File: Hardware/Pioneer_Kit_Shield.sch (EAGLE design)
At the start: 23 parts, among them J1 AVR_SPI_PRG_6NS, U1 USD-SOCKETNEW, U2 ARDUINO_R3_SHIELDNOLABELS, U3 HEX_CONVERTER

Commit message: Initial post-copy commit
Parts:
- removed J1: AVR_SPI_PRG_6NS, SparkFun-Connectors:AVR_SPI_PRG_6NS
- removed LOGO2: SFE_LOGO_FLAME.6_INCH, SparkFun-Aesthetics:SFE_LOGO_FLAME.6_INCH
- removed U$1: REVISION, SparkFun-Aesthetics:REVISION
- added C4: 0.1uF, SparkFun-Capacitors:0.1UF-0603-25V-5%
- added C5, C6: 1.0uF, SparkFun-Capacitors:1.0UF-0603-16V-10%
- added J2: (no value), SparkFun-Connectors:QWIIC_CONNECTORJS-1MM
- added JP10, JP11: FIDUCIAL1X2, SparkFun-Aesthetics:FIDUCIAL1X2
- added JP8: (no value), SparkFun-RF:XBEESMD
- added JP9: JUMPER-SMT_3_1-NC_PASTE_SILK, SparkFun-Jumpers:JUMPER-SMT_3_1-NC_PASTE_SILK
- added LED2: RED, SparkFun-LED:LED-RED0603
- added R2, R3, R4, R5: 10k, SparkFun-Resistors:10KOHM-0603-1/10W-1%
- added R6: 200k, SparkFun-Resistors:200KOHM-0603-1/10W-1%
- added R7: 1k, SparkFun-Resistors:1KOHM-0603-1/10W-1%
- added S2: (no value), SparkFun:TAC_SWITCHSMD
- added U4: PCA9306, SparkFun-IC-Comms:PCA9306PCA9306DC-1:1
- added U5: 3.3V, SparkFun-IC-Power:V_REG_AP2112K-3.3V
- C1, C2: device SparkFun-Capacitors:0.1UF-25V-5%(0603) -> SparkFun-Capacitors:0.1UF-0603-25V-5%
- C3: device SparkFun-Capacitors:10UF-6.3V-20%(0603) -> SparkFun-Capacitors:10UF-0603-6.3V-20%
- LED1: value Red -> RED; device SparkFun:LED0603 -> SparkFun-LED:LED-RED0603
- R1: device SparkFun:RESISTOR0603-RES -> SparkFun-Resistors:1KOHM-0603-1/10W-1%
- SJ1, SJ2: value SOLDERJUMPERNC -> JUMPER-SMT_2_NC_PASTE_SILK; device SparkFun-Passives:SOLDERJUMPERNC -> SparkFun-Jumpers:JUMPER-SMT_2_NC_PASTE_SILK
- U2: value ARDUINO_R3_SHIELDNOLABELS -> ARDUINO_UNO_R3_SHIELDNOLABELS; device SparkFun-Boards:ARDUINO_R3_SHIELDNOLABELS -> SparkFun-Boards:ARDUINO_UNO_R3_SHIELDNOLABELS
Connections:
- removed net CS: JP5.1, U2.D8, U3.1A
- removed net D10: JP5.3, U2.*D10
- new net !CS: JP5.3, U2.*D10, U3.1A
- new net D8: JP5.1, U2.D8
- new net N$1: LED2.C, R7.2
- new net N$19: R6.1, U4.EN, U4.VREF2
- new net N$3: JP8.DIO5, LED2.A
- new net N$5: J2.SDA, R3.1, U4.SDA1
- new net N$8: J2.SCL, R2.1, U4.SCL1
- new net N$9: JP9.2, R4.2, R5.2, R6.2
- new net TX_LV: JP8.DIN, U3.4Y
- new net VDD: C6.1, JP8.VDD, U5.OUT
- net 3.3V: now also C4.1, J2.VCC, JP9.3, R2.2, R3.2, U4.VREF1
- net 5V: now also C5.1, JP9.1, U5.EN, U5.IN; no longer J1.2
- net D7: now also S1.1
- net D9: now also S2.1
- net GND: now also C4.2, C5.2, C6.2, J2.GND, JP8.GND, R7.1, S1.3, S2.3, U4.GND, U5.GND; no longer J1.6, S1.1, S1.2
- net MISO: no longer J1.1
- net MOSI: no longer J1.4
- net RES: no longer J1.5, S1.3, S1.4, U2.RES
- net RX: now also JP8.DOUT
- net SCK: no longer J1.3
- net SCL: now also R4.1, U4.SCL2
- net SDA: now also R5.1, U4.SDA2
- net TX: now also U3.4A
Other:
- note added: "01"
- note added: "I2C/QWIIC"
- note added: "Mike Hord"
- note added: "Original uSD Shield by R Owens and T Klopfenstein"
- note added: "XBee"
- note removed: "ICSP Header"
- note removed: "Ryan Owens"
- note removed: "Toni Klopfenstein"
- note removed: "v1.4"
- moved on the sheet: C1, C2, JP4, JP5, JP6, JP7, S1, U1, U3

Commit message: Final version before review
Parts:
- removed C3: 10uF, SparkFun-Capacitors:10UF-0603-6.3V-20%
- removed SJ1, SJ2: JUMPER-SMT_2_NC_PASTE_SILK, SparkFun-Jumpers:JUMPER-SMT_2_NC_PASTE_SILK
- added C7: 22pF, SparkFun-Capacitors:22PF-0603-50V-5%
- added D1: 3A/40V/500mV, SparkFun-DiscreteSemi:DIODE-SCHOTTKY-B340A
- added FRAME2: FRAME-LETTERNO_PACKAGE, SparkFun-Aesthetics:FRAME-LETTERNO_PACKAGE
- added J1: AMP FCI 10103594-0001LF, SparkFun-Connectors:USB_MICRO-B_HALF_PTH
- added L1: 1uH, SparkFun-Coils:INDUCTOR-SRP4020-1UH
- added R8: 180k, SparkFun-Resistors:180KOHM-0603-1/10W-1%
- added R9: 820k, SparkFun-Resistors:820KOHM-0603-1/10W-1%
- C5: value 1.0uF -> 10uF; device SparkFun-Capacitors:1.0UF-0603-16V-10% -> SparkFun-Capacitors:10UF-0805-10V-10%
- C6: value 1.0uF -> 10uF; device SparkFun-Capacitors:1.0UF-0603-16V-10% -> SparkFun-Capacitors:10UF-0603-6.3V-20%
- U2: value ARDUINO_UNO_R3_SHIELDNOLABELS -> ARDUINO_UNO_R3_SHIELDUNO_R3_SHIELD_NOLABELS_LOCK; device SparkFun-Boards:ARDUINO_UNO_R3_SHIELDNOLABELS -> SparkFun-Boards:ARDUINO_UNO_R3_SHIELDUNO_R3_SHIELD_NOLABELS_LOCK
- U5: value 3.3V -> TPS62065; device SparkFun-IC-Power:V_REG_AP2112K-3.3V -> SparkFun-IC-Power:TPS62065
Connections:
- removed net D8: JP5.1, U2.D8
- removed net VDD: C6.1, JP8.VDD, U5.OUT
- new net !CD: JP5.1, U1.SHIELD@4, U2.D8
- new net N$20: C5.1, D1.C, J1.VBUS, U5.AVIN, U5.EN, U5.PVIN
- new net N$31: C7.1, R8.2, R9.1, U5.FB
- new net N$32: L1.1, U5.SW
- new net SHIELD: J1.SHIELD
- new net VCC: C6.1, C7.2, JP8.VDD, L1.2, R9.2
- net 3.3V: no longer C3.1
- net 5V: now also D1.A; no longer C5.1, U5.EN, U5.IN
- net A4: no longer SJ1.2
- net A5: no longer SJ2.2
- net GND: now also J1.GND, R8.1, U5.AGND, U5.PAD, U5.PG, U5.PGND; no longer C3.2, U1.SHIELD@2, U1.SHIELD@4, U5.GND
- net RES: now also U2.RES
- net SCL: no longer SJ2.1
- net SDA: no longer SJ1.1
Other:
- note removed: "Original uSD Shield by R Owens and T Klopfenstein"

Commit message: Changes from review
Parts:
- J2: PROD_ID (none) -> CONN-13694
- S1, S2: device SparkFun:TAC_SWITCHSMD -> SparkFun-Switches:MOMENTARY-SWITCH-SPST-2-SMD-5.2MM
- U1: PROD_ID (none) -> CONN-7820
- U3: value HEX_CONVERTER -> 74HC4050; device SparkFun:HEX_CONVERTER -> SparkFun-IC-Comms:HEX_CONVERTER
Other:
- note added: "Box intentionally empty"
- note added: "Vcc = 3.3V"
- note added: "Vsrc Select"
- moved on the sheet: JP4, JP5, JP6, JP7

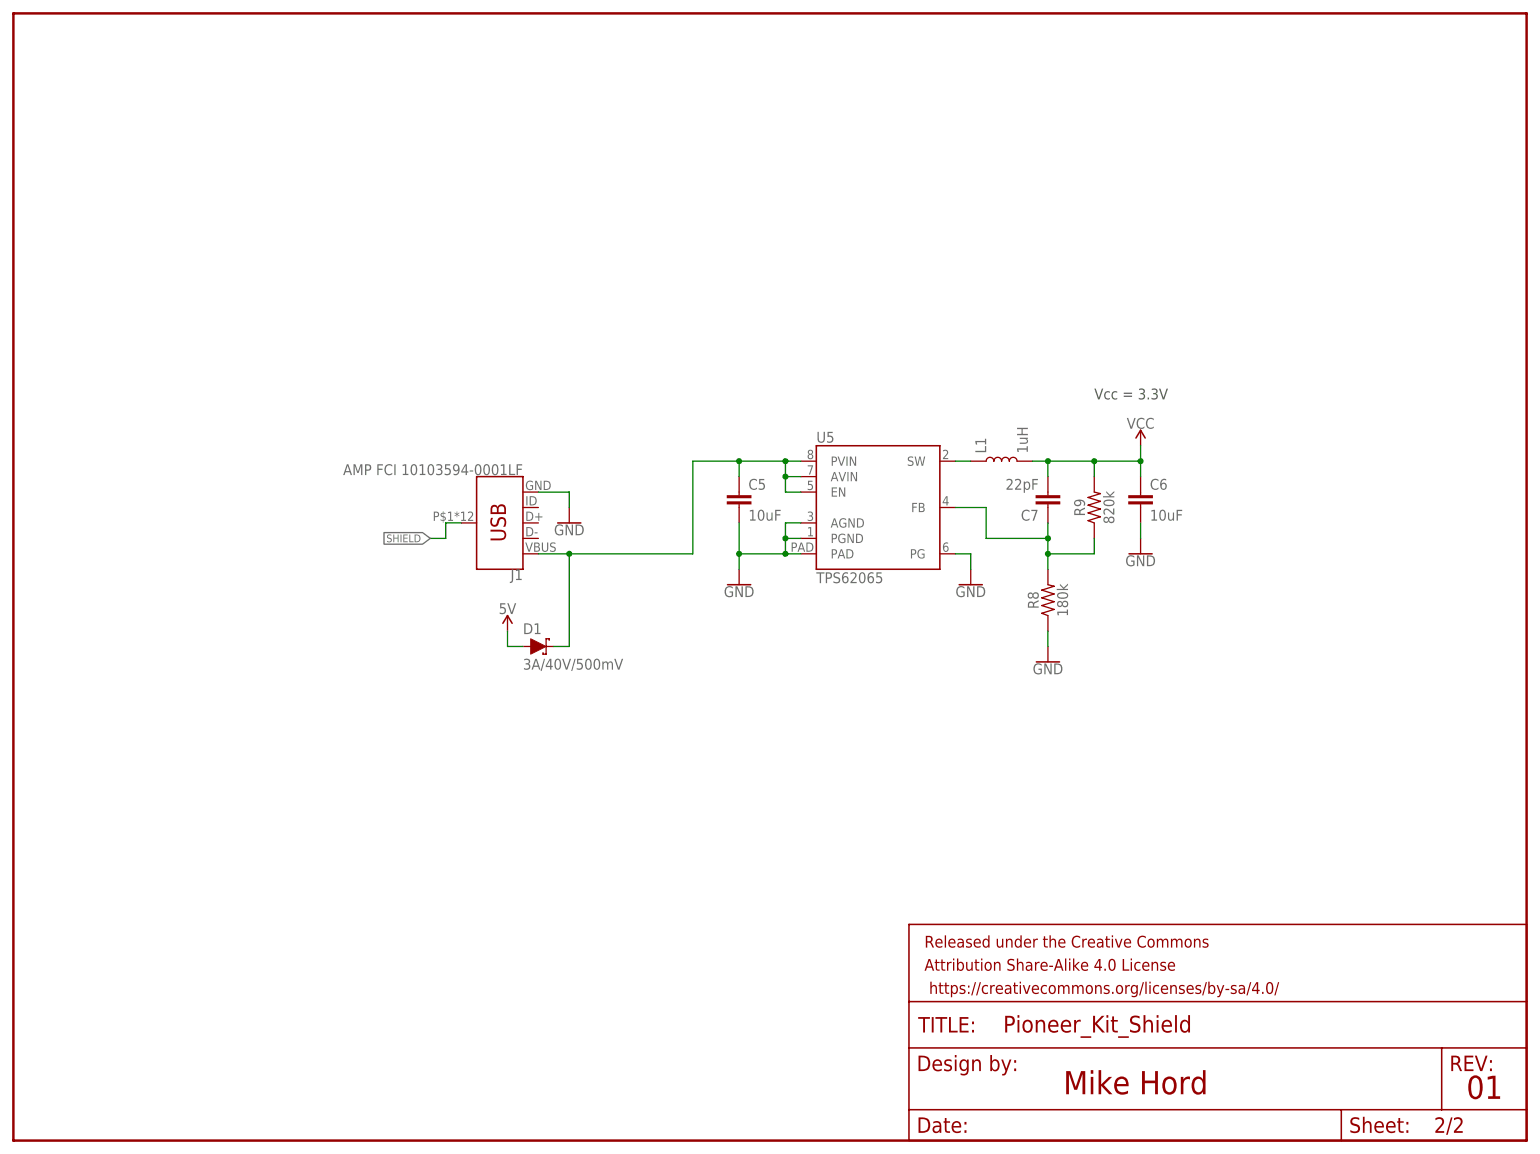
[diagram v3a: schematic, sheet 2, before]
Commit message: Fixed issues from QC double check
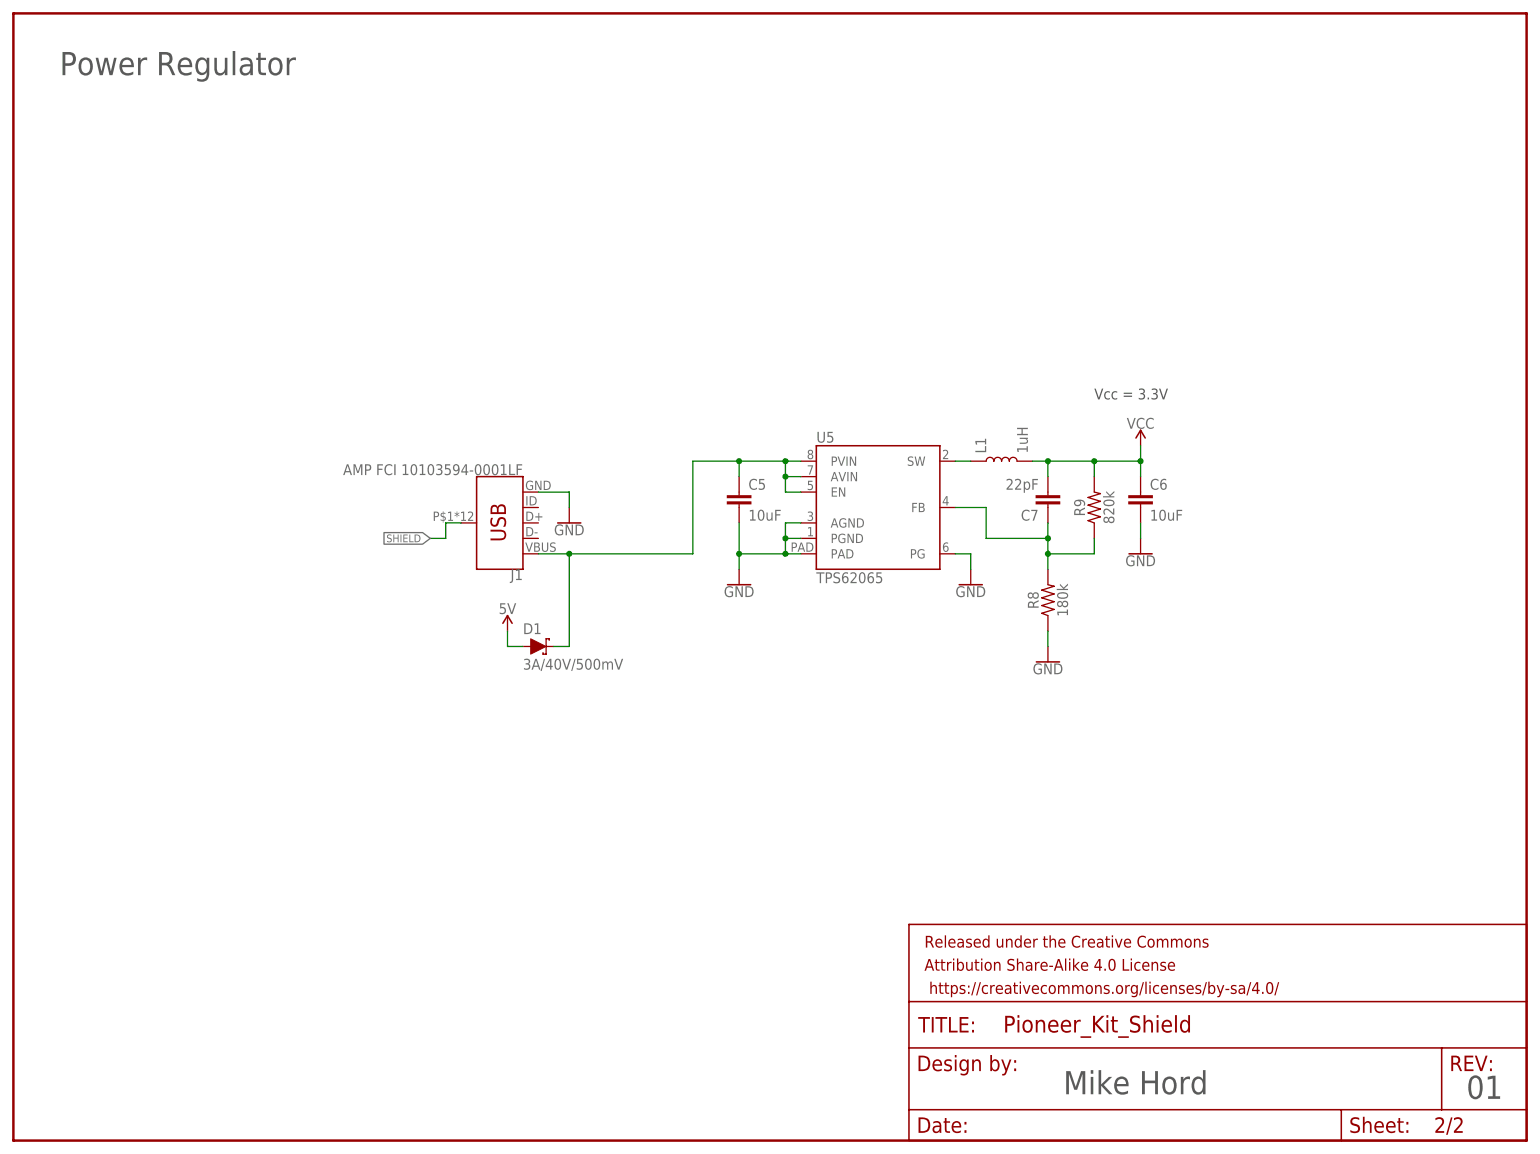
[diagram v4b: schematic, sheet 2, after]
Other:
- note added: "Power Regulator"
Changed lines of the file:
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@@
 <sheet>
 <plain>
-<text x="172.72" y="7.62" size="3.81" layer="94">Mike Hord</text>
-<text x="239.014" y="6.858" size="3.81" layer="94">01</text>
+<text x="172.72" y="7.62" size="3.81" layer="97">Mike Hord</text>
+<text x="239.014" y="6.858" size="3.81" layer="97">01</text>
 <text x="177.8" y="121.92" size="1.778" layer="97">Vcc = 3.3V</text>
+<text x="7.62" y="175.26" size="3.81" layer="97">Power Regulator</text>
 </plain>
 <instances>

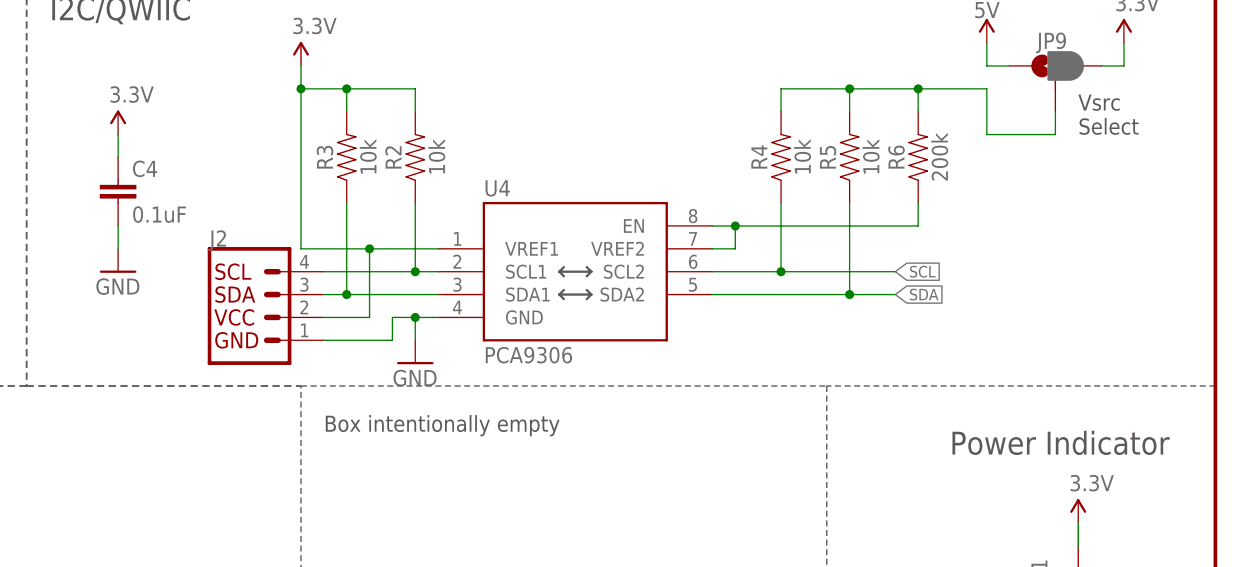
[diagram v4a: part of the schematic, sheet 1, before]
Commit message: Added testpoints
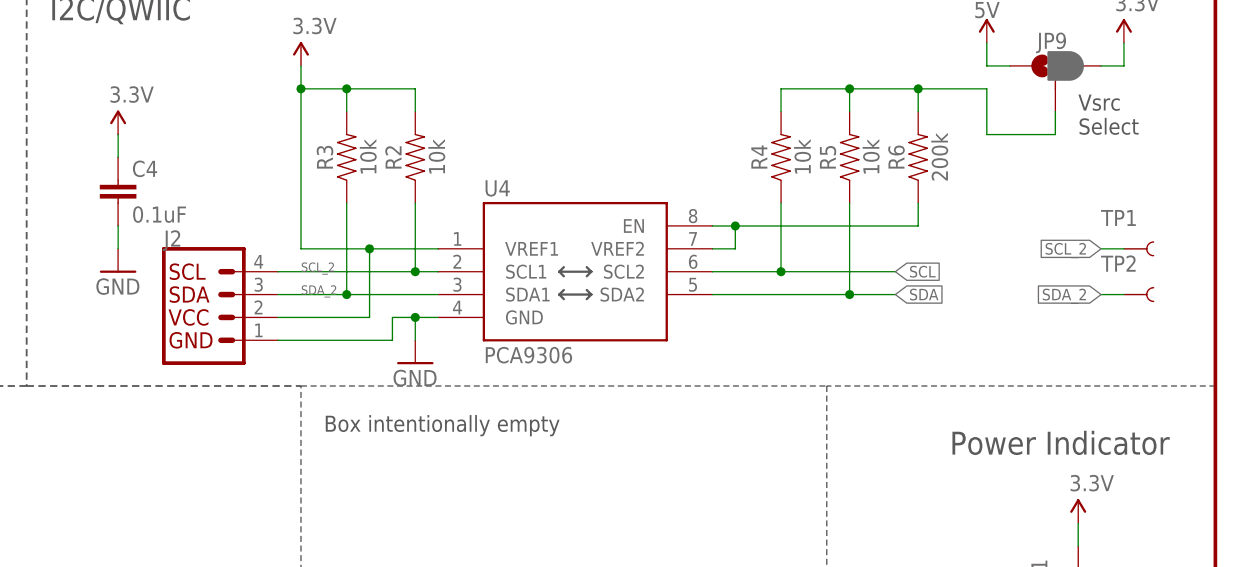
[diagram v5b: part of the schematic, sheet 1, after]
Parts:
- added TP1, TP2, TP3: TEST-POINTTP_15TH_THRU, SparkFun-Connectors:TEST-POINTTP_15TH_THRU
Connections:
- removed net N$5: J2.SDA, R3.1, U4.SDA1
- removed net N$8: J2.SCL, R2.1, U4.SCL1
- new net SCL_2: J2.SCL, R2.1, TP1.1, U4.SCL1
- new net SDA_2: J2.SDA, R3.1, TP2.1, U4.SDA1
- net VCC: now also TP3.1
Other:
- moved on the sheet: J2
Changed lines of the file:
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@@
 <part name="SUPPLY8" library="SparkFun-PowerSymbols" deviceset="VIN" device=""/>
 <part name="GND18" library="SparkFun-Aesthetics" deviceset="GND" device=""/>
+<part name="TP1" library="SparkFun-Connectors" deviceset="TEST-POINT" device="TP_15TH_THRU"/>
+<part name="TP2" library="SparkFun-Connectors" deviceset="TEST-POINT" device="TP_15TH_THRU"/>
+<part name="TP3" library="SparkFun-Connectors" deviceset="TEST-POINT" device="TP_15TH_THRU"/>
+<part name="SUPPLY9" library="SparkFun-PowerSymbols" deviceset="VCC" device=""/>
 </parts>
 <sheets>
@@
 <instance part="JP8" gate="G$1" x="114.3" y="50.8"/>
 <instance part="GND9" gate="1" x="93.98" y="33.02"/>
-<instance part="J2" gate="J1" x="142.24" y="91.44">
-<attribute name="PROD_ID" x="142.24" y="91.44" size="1.778" layer="96" display="off"/>
+<instance part="J2" gate="J1" x="137.16" y="91.44">
+<attribute name="PROD_ID" x="137.16" y="91.44" size="1.778" layer="96" display="off"/>
 </instance>
 <instance part="U4" gate="G$1" x="177.8" y="93.98"/>
@@
 <instance part="SUPPLY8" gate="G$1" x="5.08" y="22.86"/>
 <instance part="GND18" gate="1" x="22.86" y="15.24"/>
+<instance part="TP1" gate="G$1" x="238.76" y="99.06" smashed="yes">
+<attribute name="NAME" x="236.22" y="101.6" size="1.778" layer="95" font="vector"/>
+</instance>
+<instance part="TP2" gate="G$1" x="238.76" y="93.98" smashed="yes">
+<attribute name="NAME" x="236.22" y="96.52" size="1.778" layer="95" font="vector"/>
+</instance>
 </instances>
 <busses>
@@
 <junction x="152.4" y="116.84"/>
 <pinref part="J2" gate="J1" pin="VCC"/>
-<wire x1="149.86" y1="91.44" x2="154.94" y2="91.44" width="0.1524" layer="91"/>
+<wire x1="144.78" y1="91.44" x2="154.94" y2="91.44" width="0.1524" layer="91"/>
 <wire x1="154.94" y1="91.44" x2="154.94" y2="99.06" width="0.1524" layer="91"/>
 <pinref part="U4" gate="G$1" pin="VREF1"/>
@@
 <segment>
 <pinref part="J2" gate="J1" pin="GND"/>
-<wire x1="149.86" y1="88.9" x2="157.48" y2="88.9" width="0.1524" layer="91"/>
+<wire x1="144.78" y1="88.9" x2="157.48" y2="88.9" width="0.1524" layer="91"/>
 <wire x1="157.48" y1="88.9" x2="157.48" y2="91.44" width="0.1524" layer="91"/>
 <pinref part="U4" gate="G$1" pin="GND"/>
@@
 </segment>
 </net>
-<net name="N$5" class="0">
+<net name="SDA_2" class="0">
 <segment>
 <pinref part="J2" gate="J1" pin="SDA"/>
 <pinref part="U4" gate="G$1" pin="SDA1"/>
-<wire x1="149.86" y1="93.98" x2="152.4" y2="93.98" width="0.1524" layer="91"/>
+<wire x1="144.78" y1="93.98" x2="152.4" y2="93.98" width="0.1524" layer="91"/>
 <pinref part="R3" gate="G$1" pin="1"/>
 <wire x1="152.4" y1="93.98" x2="162.56" y2="93.98" width="0.1524" layer="91"/>
 <wire x1="152.4" y1="104.14" x2="152.4" y2="93.98" width="0.1524" layer="91"/>
 <junction x="152.4" y="93.98"/>
-</segment>
-</net>
-<net name="N$8" class="0">
+<label x="147.32" y="93.98" size="1.016" layer="95"/>
+</segment>
+<segment>
+<pinref part="TP2" gate="G$1" pin="1"/>
+<wire x1="238.76" y1="93.98" x2="236.22" y2="93.98" width="0.1524" layer="91"/>
+<label x="236.22" y="93.98" size="1.27" layer="95" rot="R180" xref="yes"/>
+</segment>
+</net>
+<net name="SCL_2" class="0">
 <segment>
 <pinref part="J2" gate="J1" pin="SCL"/>
 <pinref part="U4" gate="G$1" pin="SCL1"/>
-<wire x1="149.86" y1="96.52" x2="160.02" y2="96.52" width="0.1524" layer="91"/>
+<wire x1="144.78" y1="96.52" x2="160.02" y2="96.52" width="0.1524" layer="91"/>
 <pinref part="R2" gate="G$1" pin="1"/>
 <wire x1="160.02" y1="96.52" x2="162.56" y2="96.52" width="0.1524" layer="91"/>
 <wire x1="160.02" y1="104.14" x2="160.02" y2="96.52" width="0.1524" layer="91"/>
 <junction x="160.02" y="96.52"/>
+<label x="147.32" y="96.52" size="1.016" layer="95"/>
+</segment>
+<segment>
+<pinref part="TP1" gate="G$1" pin="1"/>
+<wire x1="238.76" y1="99.06" x2="236.22" y2="99.06" width="0.1524" layer="91"/>
+<label x="236.22" y="99.06" size="1.27" layer="95" rot="R180" xref="yes"/>
 </segment>
 </net>
@@
 <instance part="GND16" gate="1" x="157.48" y="91.44"/>
 <instance part="GND17" gate="1" x="185.42" y="96.52"/>
+<instance part="TP3" gate="G$1" x="220.98" y="111.76" smashed="yes">
+<attribute name="NAME" x="220.98" y="114.3" size="1.778" layer="95" font="vector"/>
+</instance>
+<instance part="SUPPLY9" gate="G$1" x="215.9" y="114.3"/>
 </instances>
 <busses>
@@
 <junction x="185.42" y="111.76"/>
 </segment>
-</net>
+<segment>
+<pinref part="SUPPLY9" gate="G$1" pin="VCC"/>
+<wire x1="215.9" y1="114.3" x2="215.9" y2="111.76" width="0.1524" layer="91"/>
+<pinref part="TP3" gate="G$1" pin="1"/>
+<wire x1="215.9" y1="111.76" x2="220.98" y2="111.76" width="0.1524" layer="91"/>
+</segment>
+</net>

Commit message: Couple of changes to v10
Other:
- note added: "10"
- note removed: "01"
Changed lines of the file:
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@@
 <wire x1="185.42" y1="129.54" x2="185.42" y2="185.42" width="0.2032" layer="97" style="shortdash"/>
 <wire x1="76.2" y1="83.82" x2="76.2" y2="0" width="0.2032" layer="97" style="shortdash"/>
-<text x="238.506" y="6.604" size="3.81" layer="97">01</text>
+<text x="238.506" y="6.604" size="3.81" layer="97">10</text>
 <text x="170.942" y="11.43" size="2.54" layer="97">Mike Hord</text>
 <text x="119.38" y="124.46" size="2.54" layer="97">I2C/QWIIC</text>
@@
 <plain>
 <text x="172.72" y="7.62" size="3.81" layer="97">Mike Hord</text>
-<text x="239.014" y="6.858" size="3.81" layer="97">01</text>
+<text x="239.014" y="6.858" size="3.81" layer="97">10</text>
 <text x="177.8" y="121.92" size="1.778" layer="97">Vcc = 3.3V</text>
 <text x="7.62" y="175.26" size="3.81" layer="97">Power Regulator</text>
